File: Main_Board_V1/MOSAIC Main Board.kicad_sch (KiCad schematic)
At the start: 82 parts, among them J1 CONN E, J10 Right Angle Qwiic Connector, J11 Vertical Qwiic Connector, J12 CONN E, J13 CONN E, J14 35RAPC4BH3 CONN 3.5MM, J2 CONN E, J3 CONN E, J4 CONN HEADER VERT 10POS 1.27MM, J5 USB TYPE C R/A SMT 16PIN, J9 CONN_JST_BATT, Q1 MOSFET P-CH 30V 3.1A SOT23-3, U1 IC SWITCH SP3T X 2 750mOhm TD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, U2 TVS DIODE 3.3VWM 6VC SOT26, U3 MCP73831 IC BATT CNTL, U4 IC REG LINEAR 3.3V 1A 8UDFN, U5 XC6503D331MR-500mA-3.3V

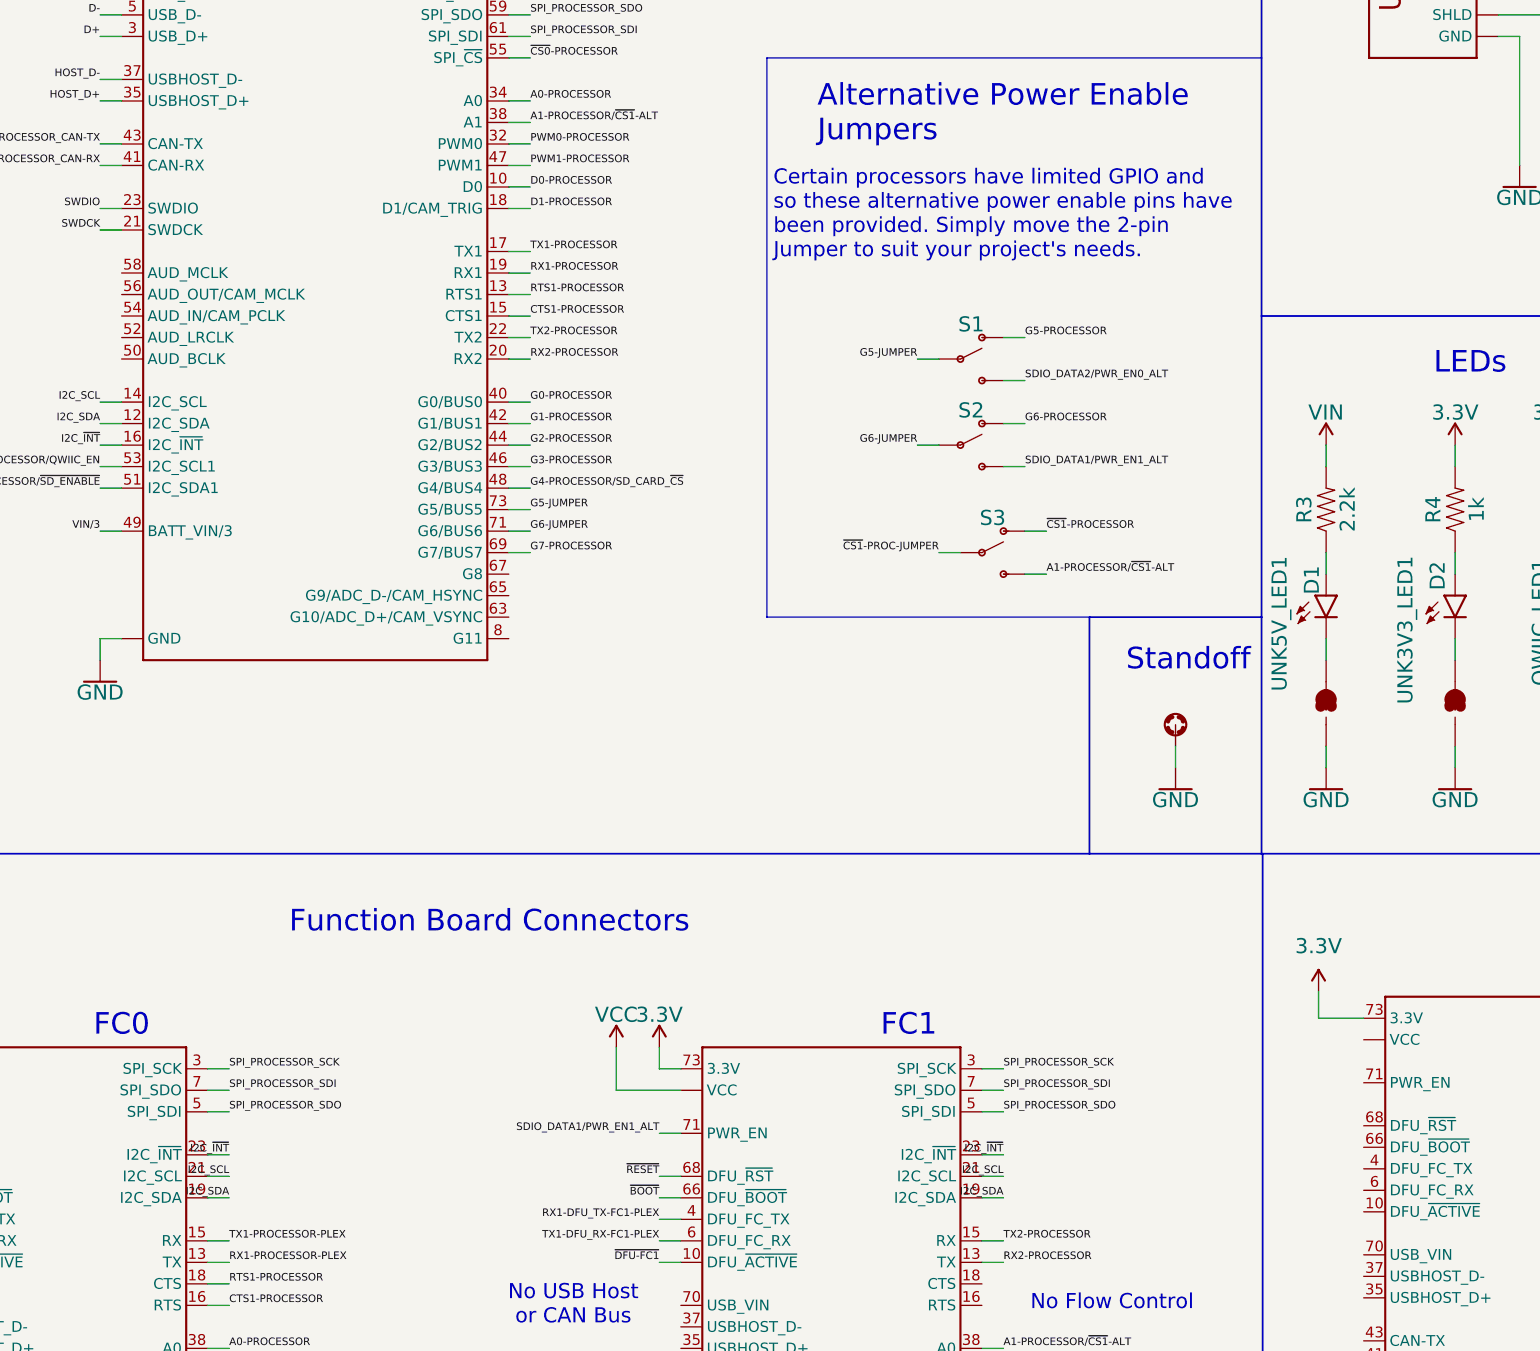
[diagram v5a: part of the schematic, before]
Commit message: board text adjustments
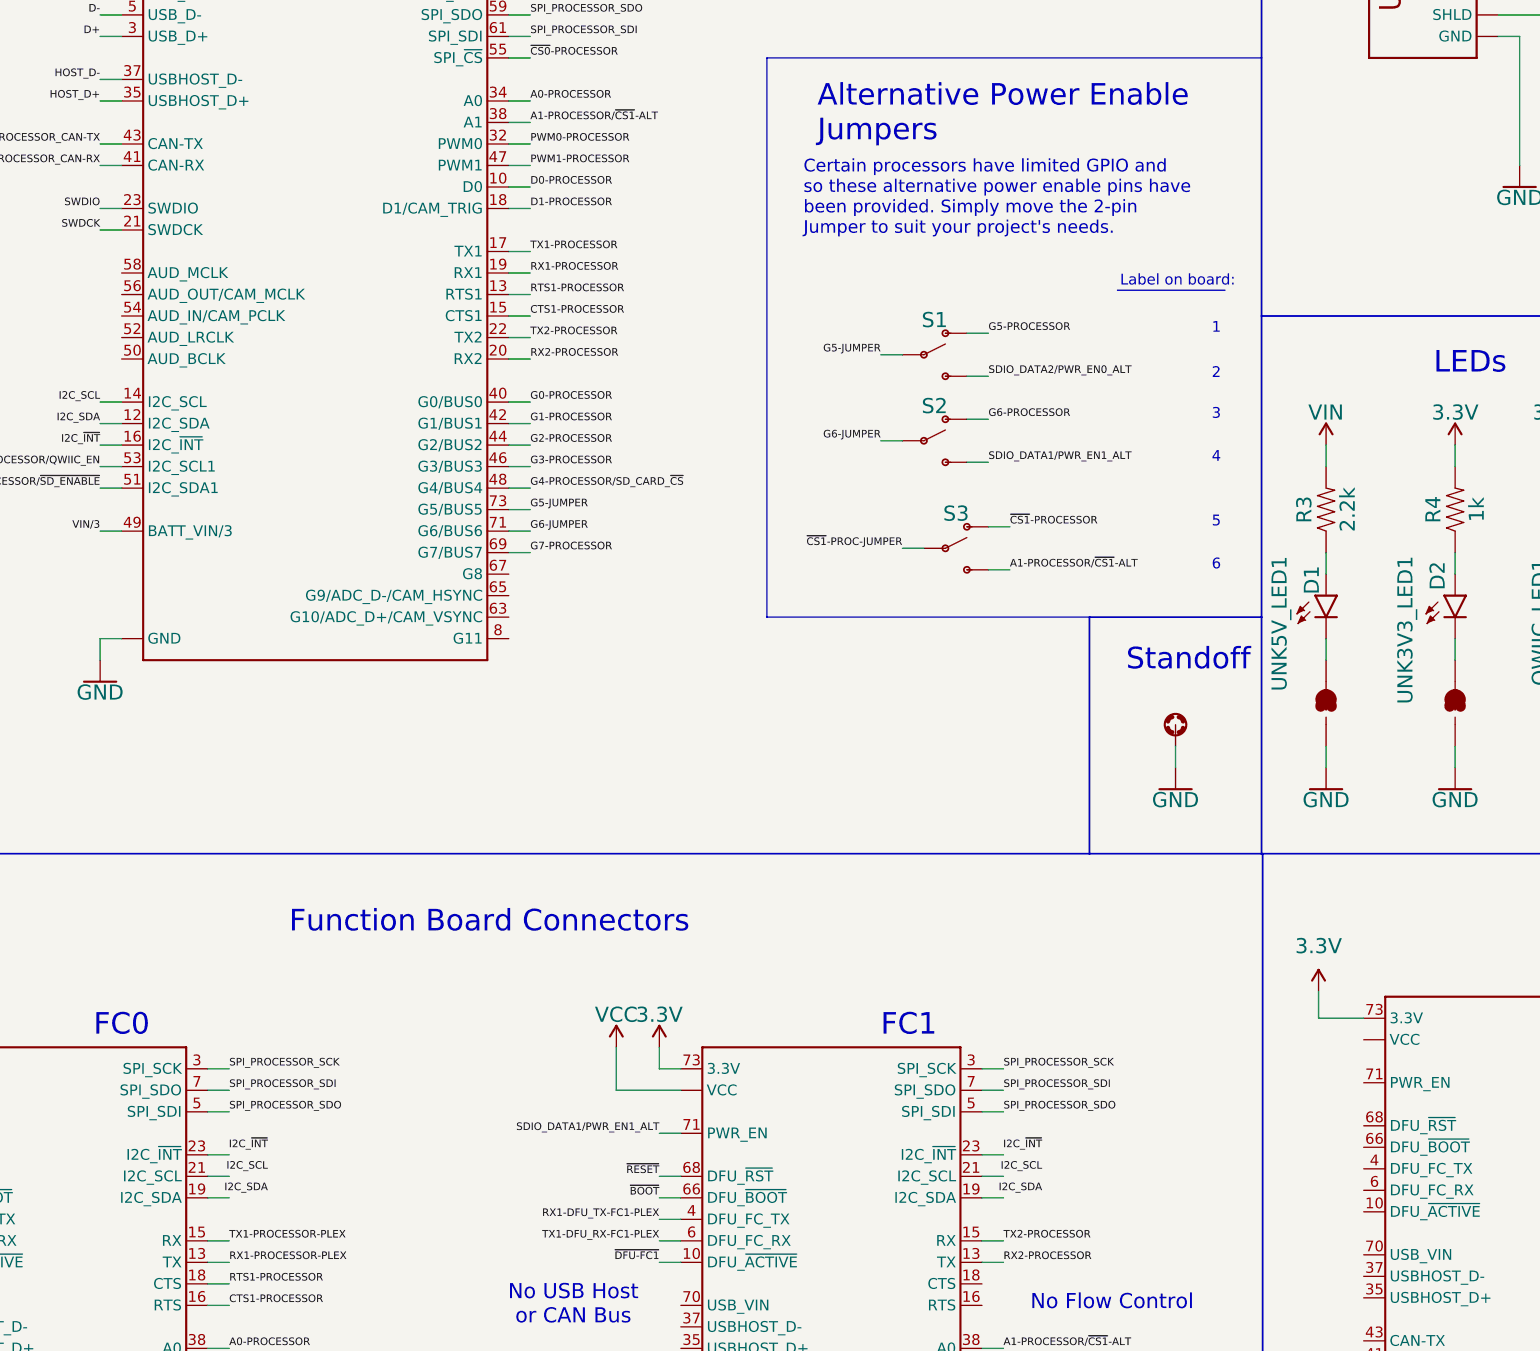
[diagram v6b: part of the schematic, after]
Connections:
- net I2C_SCL: no longer J1.21 (I2C_SCL), J3.21 (I2C_SCL)
- net I2C_SDA: no longer J1.19 (I2C_SDA), J3.19 (I2C_SDA)
- net I2C_~{INT}: no longer J1.23 (I2C_~{INT}), J3.23 (I2C_~{INT})
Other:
- note added: "1"
- note added: "2"
- note added: "3"
- note added: "4"
- note added: "5"
- note added: "6"
- note added: "Label on board:"
- moved on the sheet: S1, S2, S3
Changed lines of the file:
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@@
 		(company "Texas State Space Lab")
 	)
+	(text "Label on board:"
+		(exclude_from_sim no)
+		(at 195.072 98.044 0)
+		(effects
+			(font
+				(size 1.27 1.27)
+			)
+		)
+	)
+	(text "5"
+		(exclude_from_sim no)
+		(at 199.644 126.492 0)
+		(effects
+			(font
+				(size 1.27 1.27)
+			)
+		)
+	)
 	(text "FC1"
 		(exclude_from_sim no)
@@
 		)
 	)
+	(text "1"
+		(exclude_from_sim no)
+		(at 199.644 103.632 0)
+		(effects
+			(font
+				(size 1.27 1.27)
+			)
+		)
+	)
 	(text "Design based on SparkFun MicroMod Main Board - Double\nhttps://www.sparkfun.com/products/20595"
 		(exclude_from_sim no)
@@
 		)
 	)
+	(text "4"
+		(exclude_from_sim no)
+		(at 199.644 118.872 0)
+		(effects
+			(font
+				(size 1.27 1.27)
+			)
+		)
+	)
 	(text "Testpoints"
 		(exclude_from_sim no)
@@
 		)
 	)
+	(text "6"
+		(exclude_from_sim no)
+		(at 199.644 131.572 0)
+		(effects
+			(font
+				(size 1.27 1.27)
+			)
+		)
+	)
 	(text "Buttons"
 		(exclude_from_sim no)
@@
 		)
 	)
+	(text "2"
+		(exclude_from_sim no)
+		(at 199.644 108.966 0)
+		(effects
+			(font
+				(size 1.27 1.27)
+			)
+		)
+	)
 	(text "L"
 		(exclude_from_sim no)
@@
 		)
 	)
+	(text "3"
+		(exclude_from_sim no)
+		(at 199.644 113.792 0)
+		(effects
+			(font
+				(size 1.27 1.27)
+			)
+		)
+	)
 	(text "UART Multiplexer"
 		(exclude_from_sim no)
@@
 	(text "Certain processors have limited GPIO and\nso these alternative power enable pins have\nbeen provided. Simply move the 2-pin\nJumper to suit your project's needs."
 		(exclude_from_sim no)
-		(at 147.32 95.504 0)
+		(at 150.876 92.71 0)
 		(effects
 			(font
-				(size 1.778 1.778)
+				(size 1.5 1.5)
 			)
 			(justify left bottom)
@@
 	(wire
 		(pts
-			(xy 177.038 132.588) (xy 179.578 132.588)
+			(xy 172.72 132.08) (xy 175.26 132.08)
 		)
 		(stroke
@@
 	(wire
 		(pts
-			(xy 166.878 107.188) (xy 164.338 107.188)
+			(xy 162.56 106.68) (xy 160.02 106.68)
 		)
 		(stroke
@@
 	(wire
 		(pts
-			(xy 174.498 109.728) (xy 177.038 109.728)
+			(xy 170.18 109.22) (xy 172.72 109.22)
 		)
 		(stroke
@@
 	(wire
 		(pts
-			(xy 169.418 130.048) (xy 166.878 130.048)
+			(xy 165.1 129.54) (xy 162.56 129.54)
 		)
 		(stroke
@@
 	(wire
 		(pts
-			(xy 174.498 114.808) (xy 177.038 114.808)
+			(xy 170.18 114.3) (xy 172.72 114.3)
 		)
 		(stroke
@@
 	(wire
 		(pts
-			(xy 174.498 104.648) (xy 177.038 104.648)
+			(xy 170.18 104.14) (xy 172.72 104.14)
 		)
 		(stroke
@@
 	(wire
 		(pts
-			(xy 166.878 117.348) (xy 164.338 117.348)
+			(xy 162.56 116.84) (xy 160.02 116.84)
 		)
 		(stroke
@@
 		)
 	)
+	(polyline
+		(pts
+			(xy 187.96 99.06) (xy 200.66 99.06)
+		)
+		(stroke
+			(width 0)
+			(type default)
+		)
+	)
 	(wire
 		(pts
@@
 	(wire
 		(pts
-			(xy 177.038 127.508) (xy 179.578 127.508)
+			(xy 172.72 127) (xy 175.26 127)
 		)
 		(stroke
@@
 	(wire
 		(pts
-			(xy 174.498 119.888) (xy 177.038 119.888)
+			(xy 170.18 119.38) (xy 172.72 119.38)
 		)
 		(stroke
@@
 	)
 	(label "I2C_SCL"
-		(at 174.498 203.708 180)
+		(at 179.07 203.2 180)
 		(effects
 			(font
@@
 	)
 	(label "I2C_SDA"
-		(at 174.498 206.248 180)
+		(at 179.07 205.74 180)
 		(effects
 			(font
@@
 	)
 	(label "G6-PROCESSOR"
-		(at 177.038 114.808 0)
+		(at 172.72 114.3 0)
 		(effects
 			(font
@@
 	)
 	(label "G6-JUMPER"
-		(at 164.338 117.348 180)
+		(at 160.02 116.84 180)
 		(effects
 			(font
@@
 	)
 	(label "I2C_~{INT}"
-		(at 174.498 201.168 180)
+		(at 179.07 200.66 180)
 		(effects
 			(font
@@
 	)
 	(label "~{CS1}-PROC-JUMPER"
-		(at 166.878 130.048 180)
+		(at 162.56 129.54 180)
 		(effects
 			(font
@@
 	)
 	(label "I2C_SCL"
-		(at 83.058 203.708 180)
+		(at 87.63 203.2 180)
 		(effects
 			(font
@@
 	)
 	(label "I2C_~{INT}"
-		(at 83.058 201.168 180)
+		(at 87.63 200.66 180)
 		(effects
 			(font
@@
 	)
 	(label "G5-PROCESSOR"
-		(at 177.038 104.648 0)
+		(at 172.72 104.14 0)
 		(effects
 			(font
@@
 	)
 	(label "~{CS1}-PROCESSOR"
-		(at 179.578 127.508 0)
+		(at 175.26 127 0)
 		(effects
 			(font
@@
 	)
 	(label "A1-PROCESSOR{slash}~{CS1}-ALT"
-		(at 179.578 132.588 0)
+		(at 175.26 132.08 0)
 		(effects
 			(font
@@
 	)
 	(label "SDIO_DATA1{slash}PWR_EN1_ALT"
-		(at 177.038 119.888 0)
+		(at 172.72 119.38 0)
 		(effects
 			(font
@@
 	)
 	(label "I2C_SDA"
-		(at 83.058 206.248 180)
+		(at 87.63 205.74 180)
 		(effects
 			(font
@@
 	)
 	(label "G5-JUMPER"
-		(at 164.338 107.188 180)
+		(at 160.02 106.68 180)
 		(effects
 			(font
@@
 	)
 	(label "SDIO_DATA2/PWR_EN0_ALT"
-		(at 177.038 109.728 0)
+		(at 172.72 109.22 0)
 		(effects
 			(font
@@
 	(symbol
 		(lib_id "main_board_symbols_V1.0:SWITCH-SPDT-SMD-RIGHT-ANGLE")
-		(at 171.958 130.048 0)
+		(at 167.64 129.54 0)
 		(unit 1)
 		(exclude_from_sim no)
@@
 		(dnp no)
 		(property "Reference" "S3"
-			(at 173.228 127 0)
+			(at 168.91 126.492 0)
 			(effects
 				(font
@@
 		)
 		(property "Value" "switch"
-			(at 172.974 133.35 0)
+			(at 168.656 132.842 0)
 			(effects
 				(font
@@
 		)
 		(property "Footprint" "main_board_footprints_V1.0:SWITCH_SPST_SMD_A"
-			(at 171.958 130.048 0)
+			(at 167.64 129.54 0)
 			(effects
 				(font
@@
 		)
 		(property "Datasheet" "https://jlcpcb.com/api/file/downloadByFileSystemAccessId/8603117332785491968"
-			(at 171.958 130.048 0)
+			(at 167.64 129.54 0)
 			(effects
 				(font
@@
 		)
 		(property "Description" "https://jlcpcb.com/partdetail/Sofng-MS1290N/C19188866"
-			(at 171.958 130.048 0)
+			(at 167.64 129.54 0)
 			(effects
 				(font
@@
 		)
 		(property "JLCPCB Part #" "C19188866"
-			(at 171.958 130.048 0)
+			(at 167.64 129.54 0)
 			(effects
 				(font
@@
 		)
 		(property "FT Rotation Offset" "180"
-			(at 171.958 130.048 0)
+			(at 167.64 129.54 0)
 			(effects
 				(font
@@
 	(symbol
 		(lib_id "main_board_symbols_V1.0:SWITCH-SPDT-SMD-RIGHT-ANGLE")
-		(at 169.418 117.348 0)
+		(at 165.1 116.84 0)
 		(unit 1)
 		(exclude_from_sim no)
@@
 		(dnp no)
 		(property "Reference" "S2"
-			(at 170.688 114.3 0)
+			(at 166.37 113.792 0)
 			(effects
 				(font
@@
 		)
 		(property "Value" "switch"
-			(at 170.434 120.65 0)
+			(at 166.116 120.142 0)
 			(effects
 				(font
@@
 		)
 		(property "Footprint" "main_board_footprints_V1.0:SWITCH_SPST_SMD_A"
-			(at 169.418 117.348 0)
+			(at 165.1 116.84 0)
 			(effects
 				(font
@@
 		)
 		(property "Datasheet" "https://jlcpcb.com/api/file/downloadByFileSystemAccessId/8603117332785491968"
-			(at 169.418 117.348 0)
+			(at 165.1 116.84 0)
 			(effects
 				(font
@@
 		)
 		(property "Description" "https://jlcpcb.com/partdetail/Sofng-MS1290N/C19188866"
-			(at 169.418 117.348 0)
+			(at 165.1 116.84 0)
 			(effects
 				(font
@@
 		)
 		(property "JLCPCB Part #" "C19188866"
-			(at 169.418 117.348 0)
+			(at 165.1 116.84 0)
 			(effects
 				(font
@@
 		)
 		(property "FT Rotation Offset" "180"
-			(at 169.418 117.348 0)
+			(at 165.1 116.84 0)
 			(effects
 				(font
@@
 	(symbol
 		(lib_id "main_board_symbols_V1.0:SWITCH-SPDT-SMD-RIGHT-ANGLE")
-		(at 169.418 107.188 0)
+		(at 165.1 106.68 0)
 		(unit 1)
 		(exclude_from_sim no)
@@
 		(dnp no)
 		(property "Reference" "S1"
-			(at 170.688 104.14 0)
+			(at 166.37 103.632 0)
 			(effects
 				(font
@@
 		)
 		(property "Value" "switch"
-			(at 170.434 110.49 0)
+			(at 166.116 109.982 0)
 			(effects
 				(font
@@
 		)
 		(property "Footprint" "main_board_footprints_V1.0:SWITCH_SPST_SMD_A"
-			(at 169.418 107.188 0)
+			(at 165.1 106.68 0)
 			(effects
 				(font
@@
 		)
 		(property "Datasheet" "https://jlcpcb.com/api/file/downloadByFileSystemAccessId/8603117332785491968"
-			(at 169.418 107.188 0)
+			(at 165.1 106.68 0)
 			(effects
 				(font
@@
 		)
 		(property "Description" "https://jlcpcb.com/partdetail/Sofng-MS1290N/C19188866"
-			(at 169.418 107.188 0)
+			(at 165.1 106.68 0)
 			(effects
 				(font
@@
 		)
 		(property "JLCPCB Part #" "C19188866"
-			(at 169.418 107.188 0)
+			(at 165.1 106.68 0)
 			(effects
 				(font
@@
 		)
 		(property "FT Rotation Offset" "180"
-			(at 169.418 107.188 0)
+			(at 165.1 106.68 0)
 			(effects
 				(font

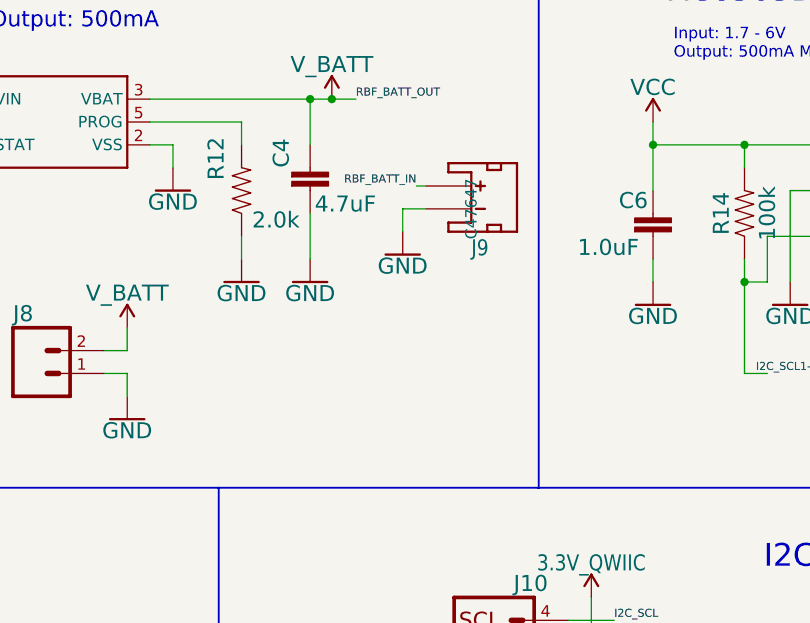
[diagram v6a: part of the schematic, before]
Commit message: fix batt input
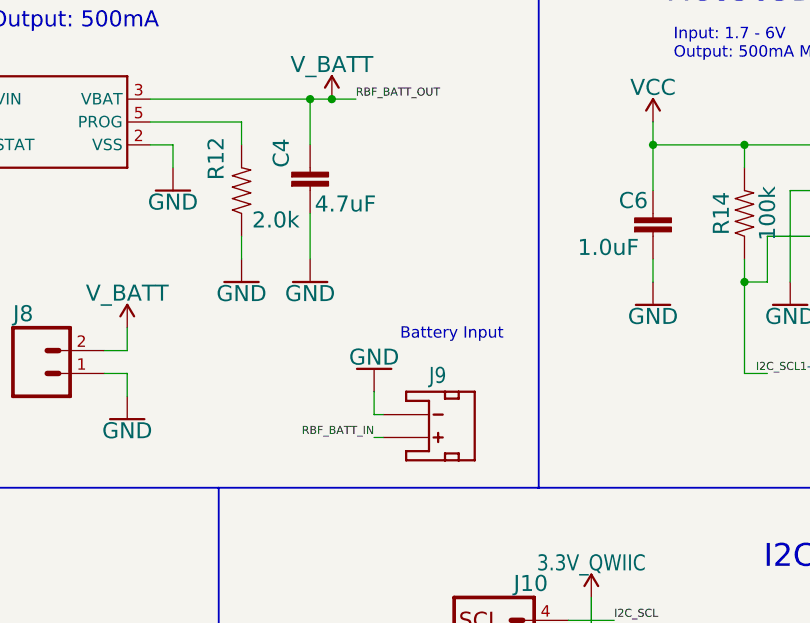
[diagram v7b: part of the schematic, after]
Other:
- note added: "Battery Input"
- moved on the sheet: J9
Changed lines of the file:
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@@
 		)
 	)
+	(text "Battery Input"
+		(exclude_from_sim no)
+		(at 373.126 148.59 0)
+		(effects
+			(font
+				(size 1.27 1.27)
+			)
+		)
+	)
 	(text "I2C - Qwiic"
 		(exclude_from_sim no)
@@
 	(wire
 		(pts
-			(xy 369.189 132.08) (xy 370.205 132.08)
+			(xy 364.49 160.02) (xy 365.506 160.02)
 		)
 		(stroke
@@
 	(wire
 		(pts
+			(xy 365.506 157.48) (xy 364.49 157.48)
+		)
+		(stroke
+			(width 0)
+			(type default)
+		)
+	)
+	(wire
+		(pts
 			(xy 410.718 132.588) (xy 413.258 132.588)
 		)
@@
 	(wire
 		(pts
-			(xy 367.665 134.62) (xy 367.665 137.16)
+			(xy 364.49 157.48) (xy 364.49 154.94)
 		)
 		(stroke
-			(width 0.1524)
-			(type solid)
+			(width 0)
+			(type default)
 		)
 	)
@@
 	(wire
 		(pts
-			(xy 370.205 134.62) (xy 367.665 134.62)
-		)
-		(stroke
-			(width 0.1524)
-			(type solid)
-		)
-	)
-	(wire
-		(pts
 			(xy 359.918 74.168) (xy 362.458 74.168)
 		)
@@
 	)
 	(label "RBF_BATT_IN"
-		(at 369.189 132.08 180)
+		(at 364.49 160.02 180)
 		(effects
 			(font
@@
 	(symbol
 		(lib_id "main_board_symbols_V1.0:JST_2MM_MALE")
-		(at 375.285 134.62 270)
-		(mirror x)
+		(at 370.586 157.48 270)
 		(unit 1)
 		(exclude_from_sim no)
@@
 		(dnp no)
 		(property "Reference" "J9"
-			(at 375.285 137.922 90)
+			(at 370.586 154.178 90)
 			(effects
 				(font
@@
 		)
 		(property "Value" "CONN_JST_BATT"
-			(at 375.285 134.62 0)
+			(at 370.586 157.48 0)
 			(effects
 				(font
@@
 		)
 		(property "Footprint" "main_board_footprints_V1.0:JST-2-SMD"
-			(at 375.285 134.62 0)
+			(at 370.586 157.48 0)
 			(effects
 				(font
@@
 		)
 		(property "Datasheet" "https://jlcpcb.com/api/file/downloadByFileSystemAccessId/8588893957006757888"
-			(at 375.285 134.62 0)
+			(at 370.586 157.48 0)
 			(effects
 				(font
@@
 		)
 		(property "Description" "https://jlcpcb.com/partdetail/48652-PH_2PSurface_Mount_RightAngle/C47647"
-			(at 375.285 134.62 0)
+			(at 370.586 157.48 0)
 			(effects
 				(font
@@
 		)
 		(property "JLCPCB Part #" "C47647"
-			(at 375.285 134.62 0)
+			(at 369.443 147.828 0)
 			(effects
 				(font
 					(size 1.27 1.27)
 				)
+				(hide yes)
 			)
 		)
@@
 	(symbol
 		(lib_id "main_board_symbols_V1.0:GND")
-		(at 367.665 139.7 0)
-		(mirror y)
+		(at 364.49 152.4 0)
+		(mirror x)
 		(unit 1)
 		(exclude_from_sim no)
@@
 		(dnp no)
 		(property "Reference" "#GND028"
-			(at 367.665 139.7 0)
+			(at 364.49 152.4 0)
 			(effects
 				(font
@@
 		)
 		(property "Value" "GND"
-			(at 367.665 139.954 0)
+			(at 364.49 152.146 0)
 			(effects
 				(font
@@
 		)
 		(property "Footprint" ""
-			(at 367.665 139.7 0)
+			(at 364.49 152.4 0)
 			(effects
 				(font
@@
 		)
 		(property "Datasheet" ""
-			(at 367.665 139.7 0)
+			(at 364.49 152.4 0)
 			(effects
 				(font
@@
 		)
 		(property "Description" ""
-			(at 367.665 139.7 0)
+			(at 364.49 152.4 0)
 			(effects
 				(font
